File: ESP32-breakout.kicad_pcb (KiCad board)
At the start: 4 copper layers, 26.4 x 49.3 mm, 56 parts, among them IC1 ESP32-S2-MINI-2U-N4, J1 UJ20-C-H-G-SMT-1-P16-TR, J2 Conn_01x03, J3 Conn_01x19, J4 Conn_01x19, Q2 Q_NMOS_DGS, SW3 SW_MEC_5E, SW4 SW_MEC_5E, U1 STUSB4500QTR, U2 TJA1051T-3, U4 TPSM33606S3QRDNRQ1, U5 STL6P3LLH6, U6 STL6P3LLH6, U7 MP9361DJ-LF-Z

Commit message: Finished V2 of the PCB
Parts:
- removed C10, C14: 2.2 uF, Capacitor_SMD:C_0603_1608Metric_Pad1.08x0.95mm_HandSolder
- removed C11: 0.47 uF, Capacitor_SMD:C_0603_1608Metric_Pad1.08x0.95mm_HandSolder
- removed C18: 4.7 uF, Capacitor_SMD:C_0603_1608Metric_Pad1.08x0.95mm_HandSolder
- removed C19: 0.1 uF, Capacitor_SMD:C_0603_1608Metric_Pad1.08x0.95mm_HandSolder
- removed C20: 1 uF, Capacitor_SMD:C_0603_1608Metric_Pad1.08x0.95mm_HandSolder
- removed C21, C22: 22 uF, Capacitor_SMD:C_0603_1608Metric_Pad1.08x0.95mm_HandSolder
- removed C6: 100nF, Capacitor_SMD:C_0603_1608Metric_Pad1.08x0.95mm_HandSolder
- removed C7, C8, C9: 1uF, Capacitor_SMD:C_0603_1608Metric_Pad1.08x0.95mm_HandSolder
- removed CR1, CR2: ESDA25P35-1U1M, Jayse_Footprints:QFN1610_STM
- removed Q2: Q_NMOS_DGS, Package_TO_SOT_SMD:SOT-23-3
- removed R14: 10k, Resistor_SMD:R_0603_1608Metric_Pad0.98x0.95mm_HandSolder
- removed R15, R7: 100k, Resistor_SMD:R_0603_1608Metric_Pad0.98x0.95mm_HandSolder
- removed R16, R17: 4.7, Resistor_SMD:R_0603_1608Metric_Pad0.98x0.95mm_HandSolder
- removed R5, R9: 1k, Resistor_SMD:R_0603_1608Metric_Pad0.98x0.95mm_HandSolder
- removed R6: 22k, Resistor_SMD:R_0603_1608Metric_Pad0.98x0.95mm_HandSolder
- removed R8: 100, Resistor_SMD:R_0603_1608Metric_Pad0.98x0.95mm_HandSolder
- removed U4: TPSM33606S3QRDNRQ1, TPSM33606S3QRDNRQ1:TPSM33606S3QRDNRQ1
- removed U5, U6: STL6P3LLH6, Jayse_Footprints:POWERFLAT_3P3X3P3_STM
- removed U7: MP9361DJ-LF-Z, Jayse_Footprints:TSOT23-6_MP9361_MNP
- C1, C17, C2, C3: footprint Capacitor_SMD:C_0603_1608Metric_Pad1.08x0.95mm_HandSolder -> Capacitor_SMD:C_01005_0402Metric
- C12, C13: footprint Capacitor_SMD:C_0603_1608Metric_Pad1.08x0.95mm_HandSolder -> Capacitor_SMD:C_01005_0402Metric; moved to F.Cu
- C4: value 4.7uF -> 1 uF; footprint Capacitor_SMD:C_0603_1608Metric_Pad1.08x0.95mm_HandSolder -> Capacitor_SMD:C_01005_0402Metric; moved to F.Cu
- C5: value 1uF -> 1 uF; footprint Capacitor_SMD:C_0603_1608Metric_Pad1.08x0.95mm_HandSolder -> Capacitor_SMD:C_01005_0402Metric; moved to F.Cu
- D1: value 1N4148WT -> SBA0520CA_R1_00001; footprint Diode_SMD:D_SOD-523 -> Package_TO_SOT_SMD:TSOT-23; moved to F.Cu
- J3, J4: value Conn_01x19 -> Conn_01x20; footprint Connector_PinHeader_2.54mm:PinHeader_1x19_P2.54mm_Vertical -> Connector_PinHeader_2.54mm:PinHeader_1x20_P2.54mm_Vertical
- R1: value 10k -> 5.1k; footprint Resistor_SMD:R_0603_1608Metric_Pad0.98x0.95mm_HandSolder -> Resistor_SMD:R_01005_0402Metric; moved to F.Cu
- R10, R13: value 165 -> 165 Ω; footprint Resistor_SMD:R_0603_1608Metric_Pad0.98x0.95mm_HandSolder -> Resistor_SMD:R_01005_0402Metric
- R11, R12: footprint Resistor_SMD:R_0603_1608Metric_Pad0.98x0.95mm_HandSolder -> Resistor_SMD:R_01005_0402Metric; moved to F.Cu
- R2: value 470 -> 5.1k; footprint Resistor_SMD:R_0603_1608Metric_Pad0.98x0.95mm_HandSolder -> Resistor_SMD:R_01005_0402Metric; moved to F.Cu
- R3, R4: footprint Resistor_SMD:R_0603_1608Metric_Pad0.98x0.95mm_HandSolder -> Resistor_SMD:R_01005_0402Metric
- U1: value STUSB4500QTR -> SL6206-33NR; footprint Package_DFN_QFN:QFN-24-1EP_4x4mm_P0.5mm_EP2.7x2.7mm -> Package_TO_SOT_SMD:TSOT-23
- moved C5 16.5 mm to (93.8, 116.5), turned to 0 degrees
- moved C4 10.9 mm to (92.7, 120.7), turned to 0 degrees
- moved D3 10.5 mm to (101.6, 122.6), turned to 180 degrees
- moved D1 8.02 mm to (92.6, 123.9), turned to 90 degrees
- moved R13 7.07 mm to (99.1, 122.9)
- moved R11 6.37 mm to (105.7, 93.9), turned to -90 degrees
- moved C12 6.03 mm to (105.0, 93.9), turned to -90 degrees
- moved C2 5.75 mm to (104.6, 89.8), turned to 90 degrees
- moved U1 5.29 mm to (92.6, 118.2), turned to 90 degrees
- moved R12 5.28 mm to (86.1, 96.5), turned to -90 degrees
- moved C13 5.10 mm to (86.8, 96.5), turned to -90 degrees
- moved C1 5.06 mm to (96.5, 91.9)
- moved D2 4.17 mm to (92.5, 112.8)
- moved R10 3.95 mm to (90.0, 113.7)
- moved R1 3.56 mm to (94.6, 128.4), turned to 90 degrees
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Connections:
- C2 pad 1: +5VCAN -> +5V
- C4 pad 1: VBUS -> +5V
- C5 pad 1: Net-(D1-K) -> +3.3V
- D1 pad 1: Net-(D1-K) -> /VBUS
- D1 pad 2: VBUS -> /VIN
- IC1 pad 11: /SDA -> /GPIO 7
- IC1 pad 12: /SCL -> /GPIO 8
- J1 pad A4_B9: VBUS -> /VBUS
- J1 pad A5: /CC1 -> Net-(J1-CC1)
- J1 pad B4_A9: VBUS -> /VBUS
- J1 pad B5: /CC2 -> Net-(J1-CC2)
- J1 pad SH2: GND -> (no net)
- J1 pad SH3: GND -> (no net)
- J1 pad SH4: GND -> (no net)
- J3 pad 10: /SDA -> /GPIO 7
- J3 pad 11: /SCL -> /GPIO 8
- J4 pad 1: /CIT_CAN- -> /CIT_CAN+
- J4 pad 2: /CIT_CAN+ -> /CIT_CAN-
- R1 pad 1: GND -> Net-(J1-CC1)
- R1 pad 2: /RESET_USB -> GND
- R2 pad 1: VBUS -> Net-(J1-CC2)
- R2 pad 2: Net-(D1-K) -> GND
- R3 pad 1: Net-(J2-Pin_3) -> /CIT_CAN-
- R3 pad 2: /CIT_CAN+ -> Net-(J2-Pin_3)
- R4 pad 1: Net-(J2-Pin_1) -> /CIT_CAN+
- R4 pad 2: /CIT_CAN- -> Net-(J2-Pin_1)
- U1 pad 1: /CC1 -> +5V
- U1 pad 2: /CC1 -> GND
- U1 pad 3: unconnected-(U1-NC-Pad3) -> +3.3V
- U2 pad 3: +5VCAN -> +5V
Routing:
- net +3.3V: track 72.6 -> 9.58 mm, vias 3 -> 6
- net +5V: track 0.00 -> 45.7 mm, vias 0 -> 3
- net /SDA: track 37.1 -> 0.00 mm, vias 2 -> 0
- net /SCL: track 37.0 -> 0.00 mm, vias 2 -> 0
- net VSINK: track 34.4 -> 0.00 mm, vias 2 -> 0
- net VBUS: track 30.8 -> 0.00 mm, vias 2 -> 0
- net +5VCAN: track 17.5 -> 0.00 mm, vias 2 -> 0
- net VBUS_EN_SNK: track 16.0 -> 0.00 mm, vias 2 -> 0
- net Net-(U5-G): track 15.5 -> 0.00 mm, vias 2 -> 0
- net /VIN: track 0.00 -> 13.2 mm
- net /BOOT: track 40.9 -> 53.9 mm, vias 3 -> 2
- net VDD_USB: track 12.5 -> 0.00 mm, vias 3 -> 0
- net /VBUS: track 0.00 -> 12.1 mm, vias 0 -> 3
- net /GPIO 8: track 0.00 -> 11.0 mm
- net /Attach: track 10.5 -> 0.00 mm, vias 2 -> 0
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- added copper zone on In2.Cu, net +3.3V
- added copper zone on In1.Cu, net GND
- added copper zone on In4.Cu, net GND
- removed copper zone on B.Cu, net GND
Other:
- board size 26.4 x 49.3 mm -> 26.4 x 51.8 mm
- copper layers 4 -> 6

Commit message: Changed power system and added ESD protection
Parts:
- added C10: 2.2 uF, Capacitor_SMD:C_01005_0402Metric, B.Cu at (90.6, 88.7)
- added C11: 0.47 uF, Capacitor_SMD:C_01005_0402Metric, F.Cu at (87.3, 87.4)
- added C6: 1 uF, Capacitor_SMD:C_01005_0402Metric, F.Cu at (91.0, 120.8)
- added C7: 22 uF, Capacitor_SMD:C_01005_0402Metric, F.Cu at (95.2, 115.7)
- added C8: 4.7 uF, Capacitor_SMD:C_01005_0402Metric, F.Cu at (95.5, 119.5)
- added C9: 100 nF, Capacitor_SMD:C_01005_0402Metric, F.Cu at (95.5, 118.9)
- added D4: SM15NB, Package_TO_SOT_SMD:SOT-23-3, B.Cu at (96.4, 126.8)
- added R5: 33.2k, Resistor_SMD:R_01005_0402Metric, F.Cu at (92.1, 121.0)
- added R6: 14.3k, Resistor_SMD:R_01005_0402Metric, F.Cu at (93.1, 121.0)
- added U3: TPSM33606S3QRDNRQ1, TPSM33606S3QRDNRQ1:TPSM33606S3QRDNRQ1, F.Cu at (92.6, 117.7)
- C4: value 1 uF -> 2.2 uF; moved to B.Cu
- C5: value 1 uF -> 22 uF
- U1: value SL6206-33NR -> MP9361DJ-LF-Z; footprint Package_TO_SOT_SMD:TSOT-23 -> Jayse_Footprints:TSOT23-6_MP9361_MNP
- moved C4 33.3 mm to (90.7, 87.4), turned to -90 degrees
- moved U1 30.4 mm to (89.8, 88.0), turned to 180 degrees
- moved C5 1.65 mm to (94.2, 114.9)
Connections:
- C4 pad 1: +5V -> +3.3V
- D1 pad 2: /VIN -> /VIN_PIN
- D1 pad 3: +5V -> /VIN
- J3 pad 20: /VIN -> /VIN_PIN
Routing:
- net +5V: track 45.7 -> 14.7 mm, vias 3 -> 2
- net /VIN_PIN: track 0.00 -> 13.2 mm
- net GND: track 18.8 -> 25.9 mm, vias 28 -> 33
- net /VIN: track 13.2 -> 7.37 mm, vias 0 -> 1
- net +3.3V: track 9.58 -> 13.1 mm, vias 6 -> 11
- net Net-(U1-CP): track 0.00 -> 2.28 mm
- net Net-(U3-FB): track 0.00 -> 2.22 mm
- net Net-(U3-VCC): track 0.00 -> 1.44 mm
- net Net-(U1-CN): track 0.00 -> 1.22 mm
- net /D-: track 25.5 -> 26.2 mm, vias 0 -> 1
- net /D+: track 26.4 -> 27.0 mm, vias 0 -> 1

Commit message: Changed capacitors and ESD diodes, began revisions
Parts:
- removed D4: SM15NB, Package_TO_SOT_SMD:SOT-23-3
- added C14: 1 nF, Capacitor_SMD:C_0402_1005Metric, F.Cu at (90.3, 118.4)
- added C15: 1 nF, Capacitor_SMD:C_0402_1005Metric, F.Cu at (87.5, 98.5)
- added D5: TPD1E05U06QDPYRQ1, Diode_SMD:D_0603_1608Metric, F.Cu at (97.9, 112.8)
- added D6: TPD1E05U06QDPYRQ1, Diode_SMD:D_0603_1608Metric, F.Cu at (94.7, 112.8)
- added D7: TPD1E05U06QDPYRQ1, Diode_SMD:D_0603_1608Metric, F.Cu at (80.6, 76.7)
- added D8: TPD1E05U06QDPYRQ1, Diode_SMD:D_0603_1608Metric, F.Cu at (81.8, 81.6)
- C1, C10, C17, C2, C3, C4: footprint Capacitor_SMD:C_01005_0402Metric -> Capacitor_SMD:C_0402_1005Metric; moved to F.Cu
- C11, C12, C13, C5, C6, C7: footprint Capacitor_SMD:C_01005_0402Metric -> Capacitor_SMD:C_0402_1005Metric
- C8: footprint Capacitor_SMD:C_01005_0402Metric -> Capacitor_SMD:C_1206_3216Metric
- C9: value 100 nF -> 4.7 uF; footprint Capacitor_SMD:C_01005_0402Metric -> Capacitor_SMD:C_1206_3216Metric
- R1, R10, R11, R12, R13, R2, R5, R6: footprint Resistor_SMD:R_01005_0402Metric -> Resistor_SMD:R_0402_1005Metric
- R3, R4: footprint Resistor_SMD:R_01005_0402Metric -> Resistor_SMD:R_0402_1005Metric; moved to F.Cu
- U2: moved to F.Cu
- moved D2 16.6 mm to (102.0, 126.4)
- moved R10 15.7 mm to (99.3, 126.4), turned to -90 degrees
- moved C6 8.34 mm to (89.5, 112.6)
- moved R5 8.11 mm to (87.5, 114.3), turned to -90 degrees
- moved R6 7.28 mm to (87.5, 116.4)
- moved C1 7.28 mm to (102.2, 87.4)
- moved D3 6.71 mm to (94.9, 122.8), turned to 90 degrees
- moved C8 5.94 mm to (91.3, 123.7)
- moved C11 5.53 mm to (88.8, 82.1)
- moved D1 5.38 mm to (88.5, 127.4)
- moved R13 5.38 mm to (94.9, 119.6), turned to -90 degrees
- moved C9 4.65 mm to (91.3, 121.0)
- moved C13 4.39 mm to (86.5, 92.1)
- moved SW4 4.03 mm to (102.0, 121.9)
- moved C17 3.77 mm to (86.4, 98.5)
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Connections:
- D1 pad 1: /VBUS -> /VIN_PIN
- D1 pad 2: /VIN_PIN -> /VBUS
- IC1 pad 22: /LED -> /GPIO 18
- IC1 pad 29: /GPIO 34 -> /LED
- J1 pad SH2: (no net) -> GND
- J1 pad SH3: (no net) -> GND
- J1 pad SH4: (no net) -> GND
- J4 pad 14: /GPIO 34 -> /LED
- J4 pad 18: /LED -> /GPIO 18
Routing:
- net /BOOT: track 53.9 -> 4.15 mm, vias 2 -> 0
- net /LED: track 35.0 -> 0.00 mm, vias 1 -> 0
- net /GPIO 17: track 31.4 -> 0.00 mm, vias 1 -> 0
- net /GPIO 16: track 29.1 -> 0.00 mm, vias 1 -> 0
- net /GPIO 21: track 28.4 -> 0.00 mm
- net /GPIO 15: track 26.2 -> 0.00 mm, vias 1 -> 0
- net /EN: track 29.1 -> 4.15 mm, vias 2 -> 0
- net GND: track 25.9 -> 1.07 mm, vias 33 -> 20
- net /GPIO 26: track 24.4 -> 0.00 mm
- net /GPIO 14: track 23.4 -> 0.00 mm
- net /GPIO 13: track 20.5 -> 0.00 mm
- net /GPIO 33: track 18.3 -> 0.00 mm, vias 1 -> 0
- net /GPIO 12: track 17.6 -> 0.00 mm
- net /CIT_CAN-: track 16.2 -> 0.00 mm
- net /GPIO 11: track 15.9 -> 0.00 mm, vias 1 -> 0
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- added copper zone on F.Cu, net /VIN
- removed copper zone on In2.Cu, net +3.3V

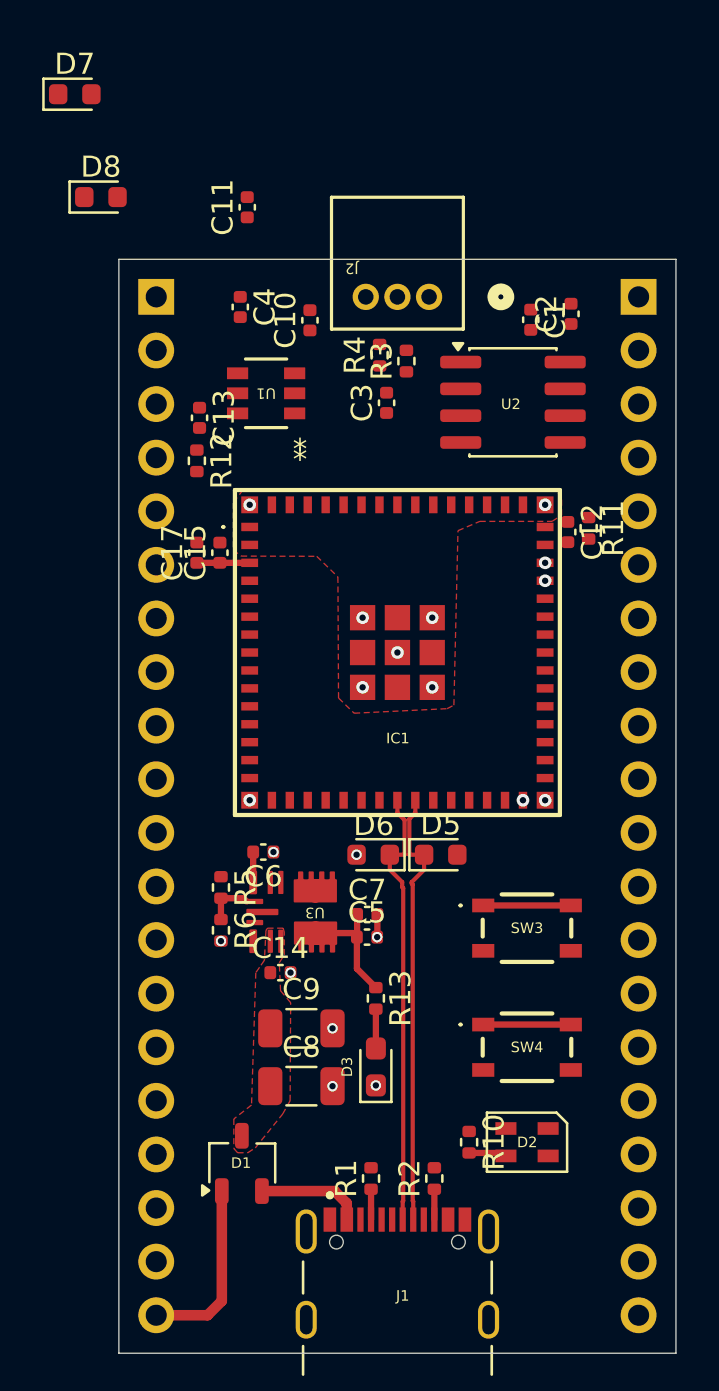
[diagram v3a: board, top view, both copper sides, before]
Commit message: Routed the new board design
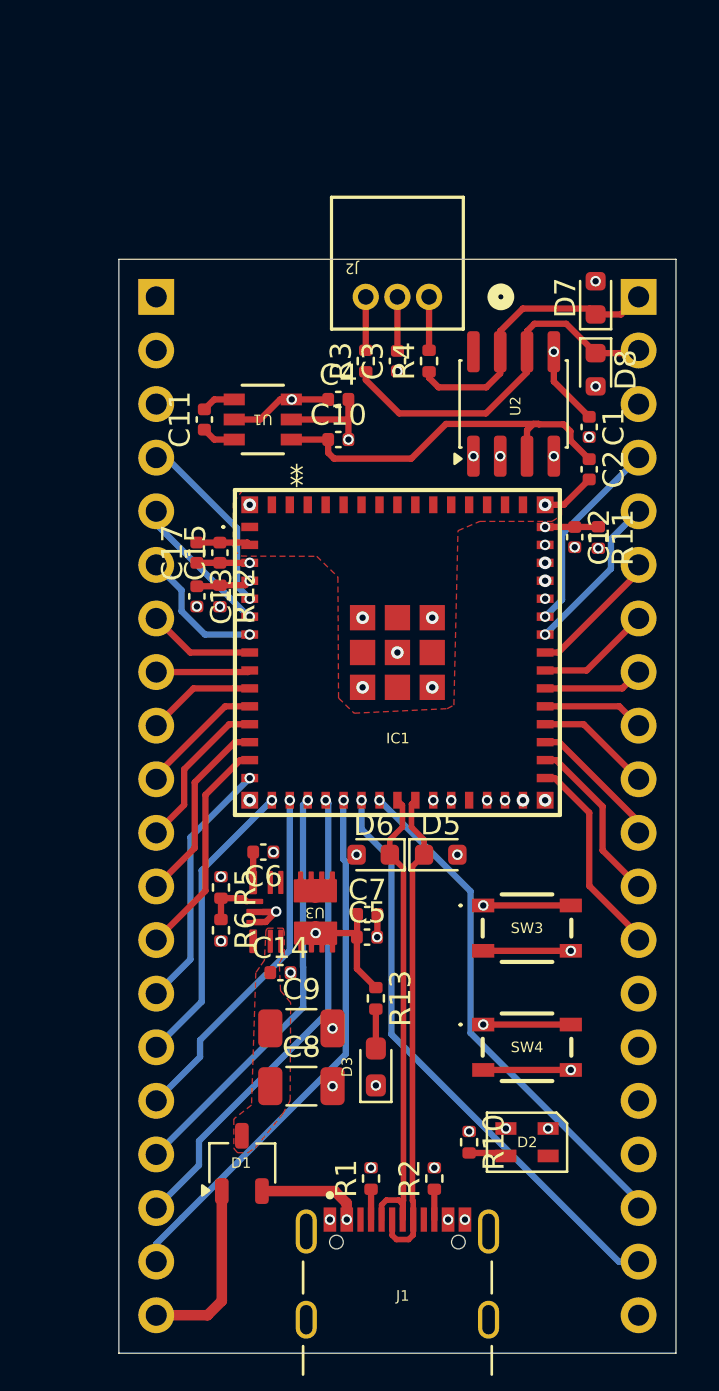
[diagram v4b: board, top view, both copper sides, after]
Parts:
- moved D7 26.5 mm to (105.3, 86.4), turned to 90 degrees
- moved D8 24.8 mm to (105.3, 89.8), turned to -90 degrees
- moved C11 10.3 mm to (86.7, 92.2)
- moved C13 8.46 mm to (86.4, 100.5)
- moved C2 7.42 mm to (105.0, 94.5), turned to -90 degrees
- moved R12 6.50 mm to (87.5, 100.5)
- moved C4 6.39 mm to (93.1, 91.2), turned to 0 degrees
- moved C10 5.81 mm to (93.1, 93.1), turned to 0 degrees
- moved C1 5.79 mm to (105.0, 92.5)
- moved R4 2.36 mm to (97.4, 89.4)
- moved C3 2.05 mm to (95.9, 89.4)
- moved R3 1.93 mm to (94.4, 89.4)
- moved U1 1.25 mm to (89.5, 92.2)
- moved R11 0.63 mm to (105.4, 97.7)
- moved C12 0.41 mm to (104.3, 97.7)
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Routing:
- net +3.3V: track 8.38 -> 90.2 mm, vias 0 -> 8
- net /BOOT: track 4.15 -> 42.6 mm, vias 0 -> 2
- net /EN: track 4.15 -> 33.8 mm, vias 0 -> 2
- net /GPIO 17: track 0.00 -> 27.9 mm, vias 0 -> 1
- net /GPIO 16: track 0.00 -> 25.6 mm, vias 0 -> 1
- net /GPIO 18: track 0.00 -> 24.4 mm, vias 0 -> 1
- net /GPIO 15: track 0.00 -> 22.8 mm, vias 0 -> 1
- net /LED: track 0.00 -> 22.6 mm, vias 0 -> 2
- net /GPIO 21: track 0.00 -> 22.1 mm, vias 0 -> 1
- net GND: track 1.07 -> 21.0 mm, vias 20 -> 37
- net /GPIO 14: track 0.00 -> 19.8 mm, vias 0 -> 1
- net +5V: track 0.00 -> 18.4 mm
- net /GPIO 26: track 0.00 -> 17.9 mm, vias 0 -> 1
- net /CIT_CAN-: track 0.00 -> 17.5 mm
- net /GPIO 13: track 0.00 -> 16.9 mm, vias 0 -> 1
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
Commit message: Finished revisions and silkscreen
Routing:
- net GND: track 21.0 -> 24.2 mm, vias 37 -> 36
- net /BOOT: track 42.6 -> 44.9 mm
- net /GPIO 16: track 25.6 -> 26.9 mm
- net /EN: track 33.8 -> 34.8 mm
- net /GPIO 44: track 9.37 -> 10.1 mm
- net /GPIO 11: track 12.1 -> 12.8 mm
- net /LED: track 22.6 -> 23.3 mm
